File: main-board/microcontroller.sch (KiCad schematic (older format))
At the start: 40 parts, among them J1 ECS00065

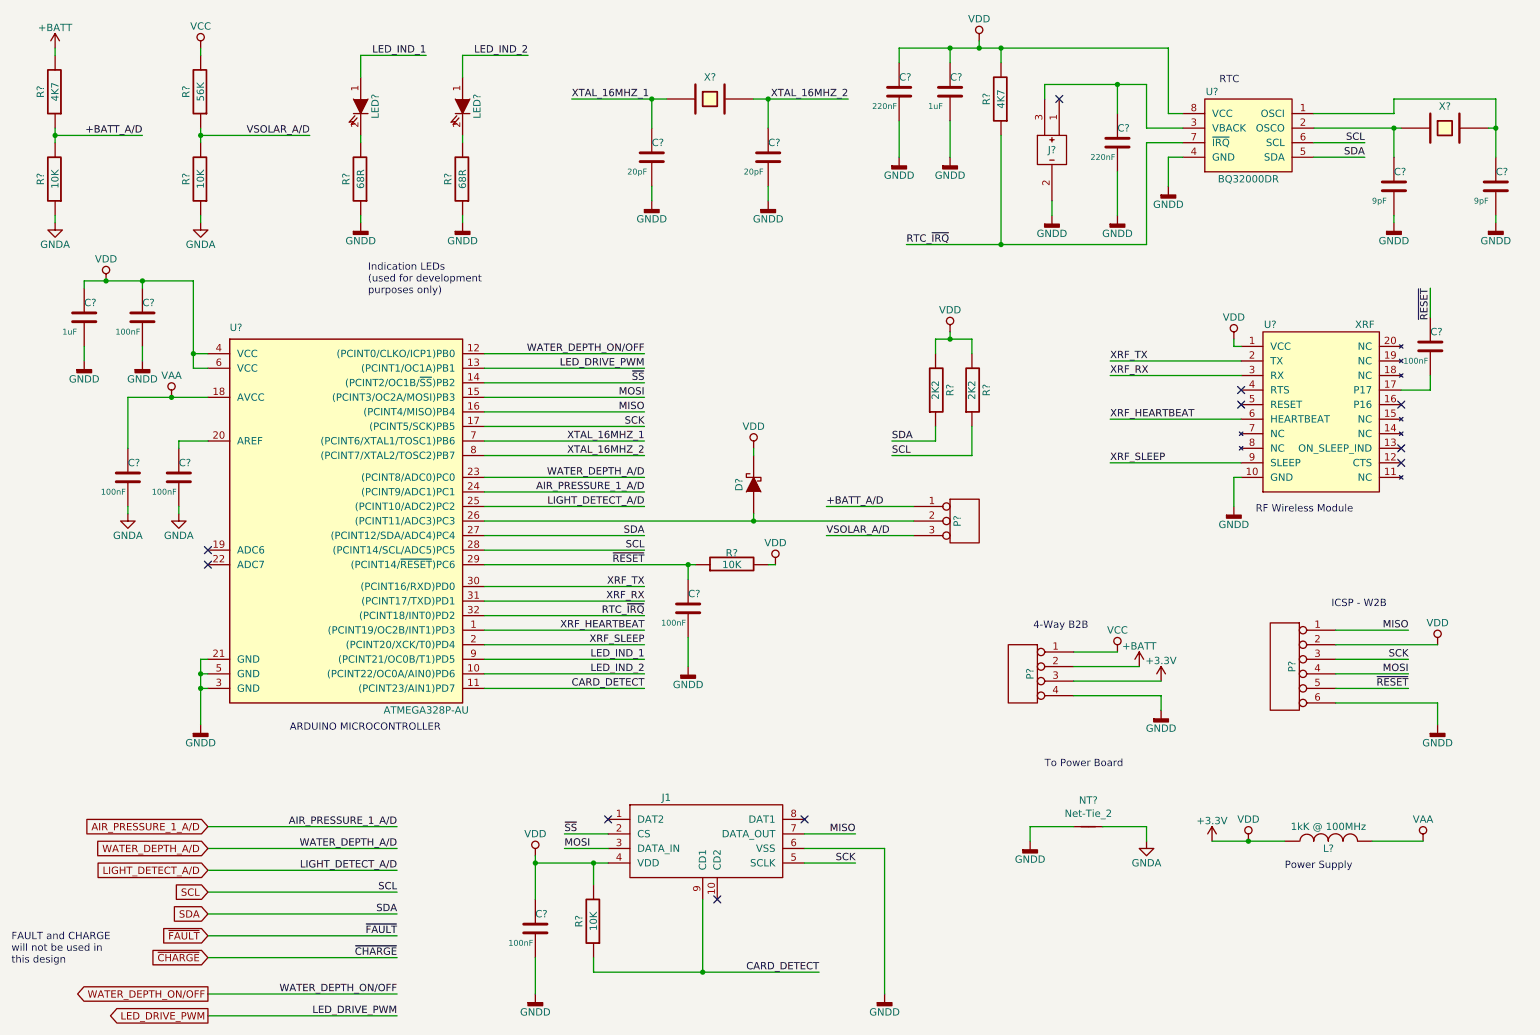
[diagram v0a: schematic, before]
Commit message: Added output files, gerbers, dril files, raster images, and updates to PCB design files.
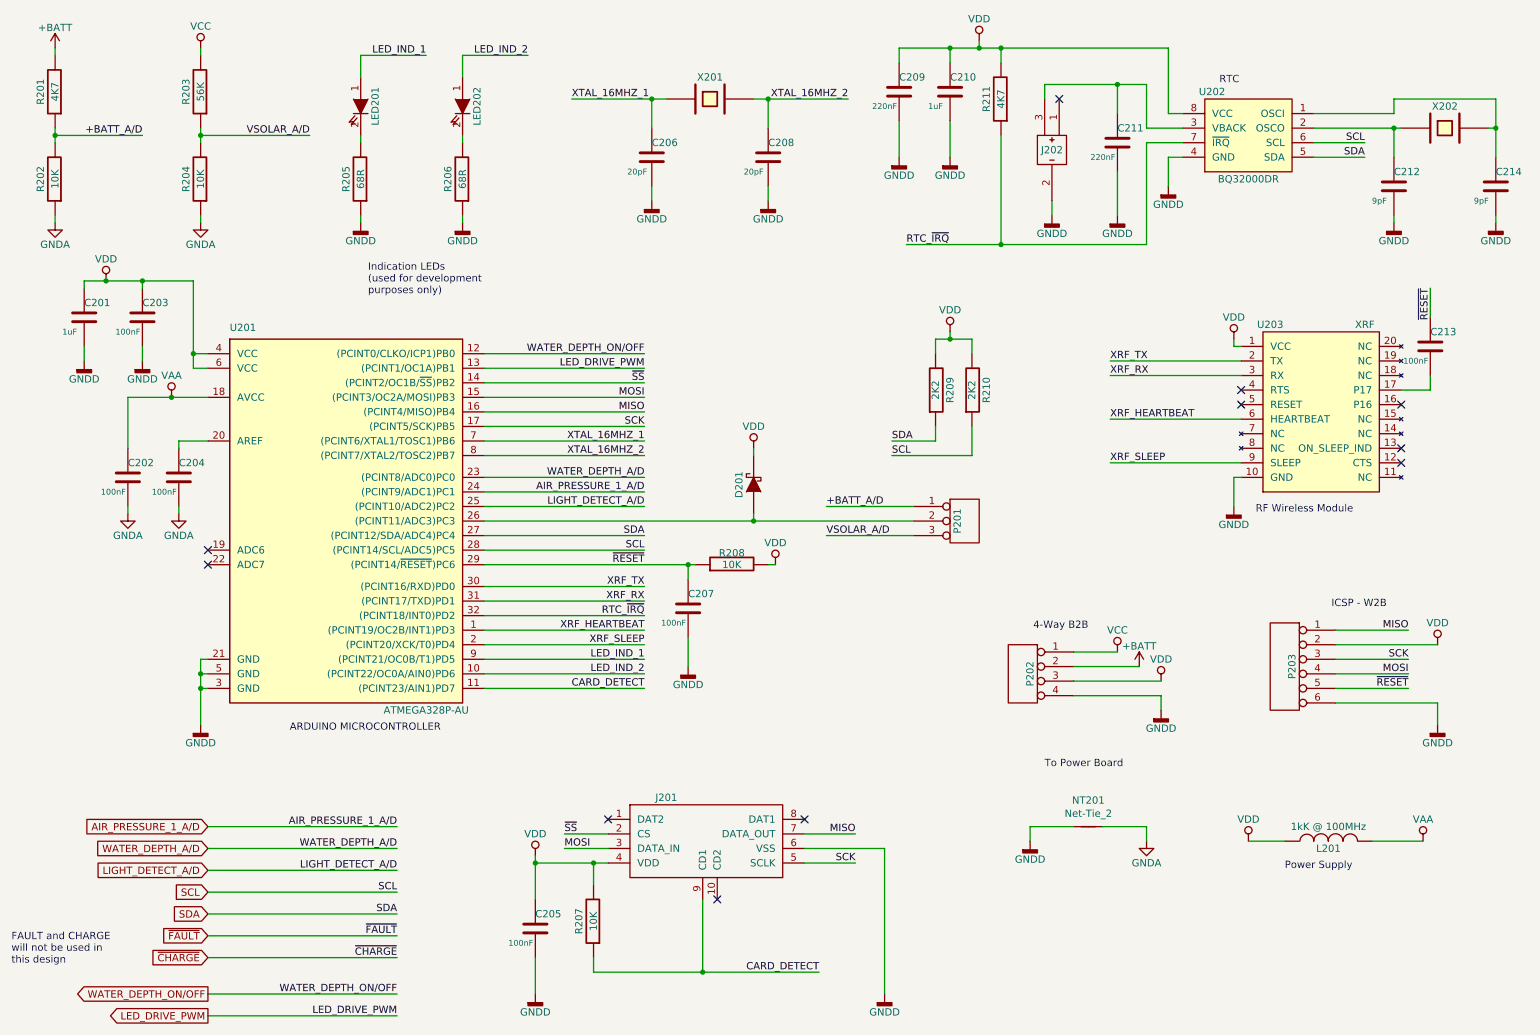
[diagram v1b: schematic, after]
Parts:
- gave numbers to parts that had none: 39
- renumbered J1 to J201
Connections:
- net +3V3 renamed VDD
